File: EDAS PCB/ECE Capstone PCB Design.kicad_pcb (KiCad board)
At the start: 2 copper layers, 149.1 x 102.3 mm, 86 parts, among them J1 1053131105, J2 1053131105, J3 Conn_01x40_Socket, U1 MCP2518FDT-H/SL, U2 MCP2542FD-E/SN, U5 TPS562201, U6 TPS61165DBV, U7 TPS562201

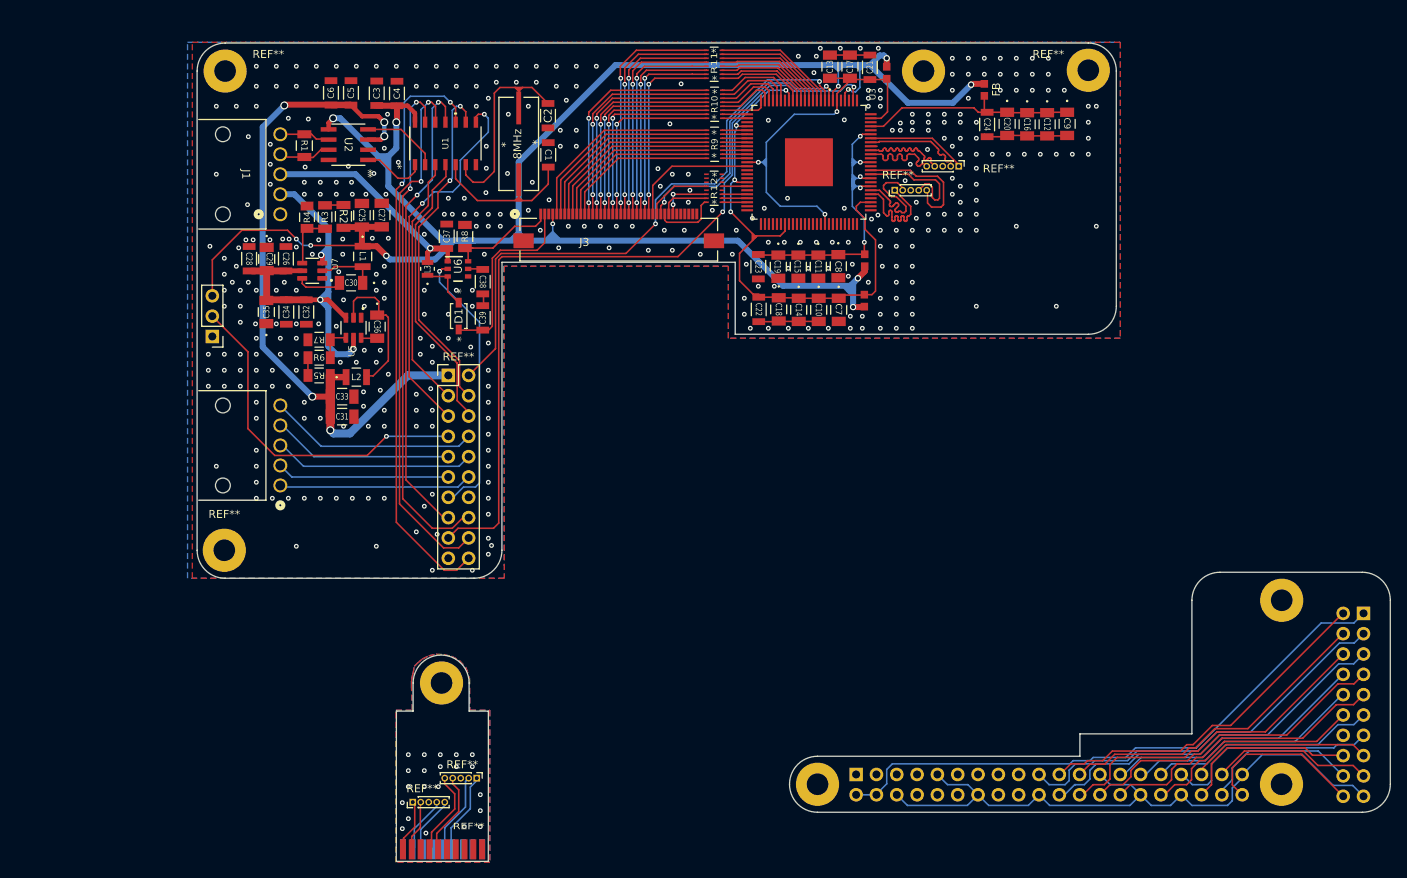
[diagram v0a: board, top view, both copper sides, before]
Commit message: Found a problem with one of the HDMI traces where the same net track spacing was to small. Corrected
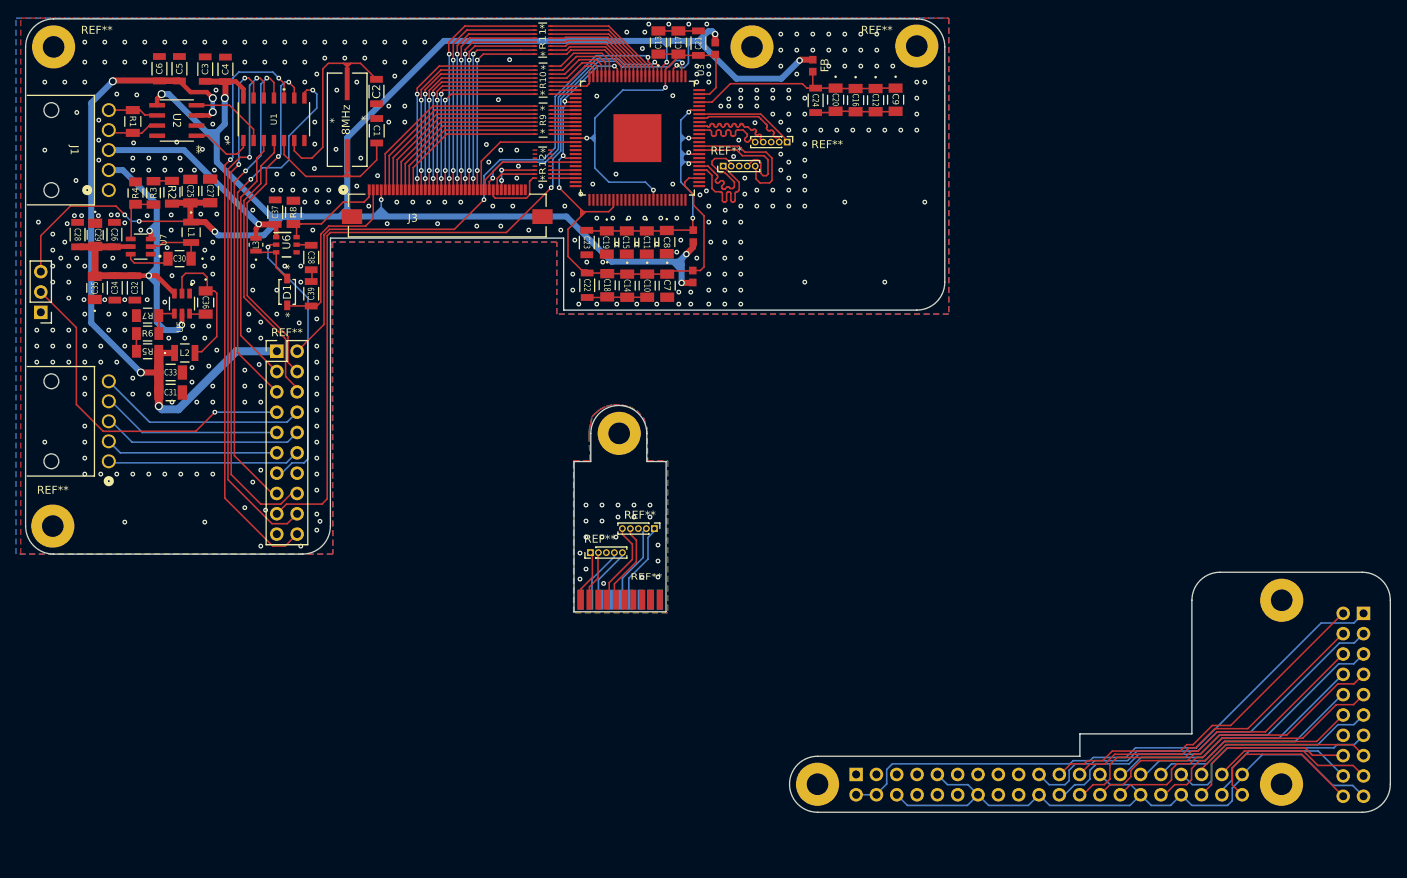
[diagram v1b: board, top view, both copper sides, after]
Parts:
- removed the ? at (153.1, 127.1)
- removed the ? at (213.4, 50.6)
- removed the REF** at (217.8, 62.5)
- removed the REF** at (149.6, 142.0)
- removed the REF** at (126.1, 50.6)
- removed the REF** at (157.6, 139.0)
- removed the REF** at (234.0, 50.5)
- removed the REF** at (209.8, 65.5)
- removed the REF** at (126.0, 110.5)
- added ?: , , F.Cu at (175.3, 95.9)
- added ?: , , F.Cu at (192.0, 47.6)
- added REF**: MountingHole_2.7mm_M2.5_Pad, MountingHole:MountingHole_2.7mm_M2.5_Pad, F.Cu at (212.6, 47.5)
- added REF**: MountingHole_2.7mm_M2.5_Pad, MountingHole:MountingHole_2.7mm_M2.5_Pad, F.Cu at (104.6, 107.5)
- added REF**: PinHeader_1x05_P1.00mm_Vertical, Connector_PinHeader_1.00mm:PinHeader_1x05_P1.00mm_Vertical, F.Cu at (188.4, 62.5)
- added REF**: PinHeader_1x05_P1.00mm_Vertical, Connector_PinHeader_1.00mm:PinHeader_1x05_P1.00mm_Vertical, F.Cu at (179.8, 107.8)
- added REF**: PinHeader_1x05_P1.00mm_Vertical, Connector_PinHeader_1.00mm:PinHeader_1x05_P1.00mm_Vertical, F.Cu at (171.8, 110.8)
- added REF**: MountingHole_2.7mm_M2.5_Pad, MountingHole:MountingHole_2.7mm_M2.5_Pad, F.Cu at (104.7, 47.6)
- added REF**: PinHeader_1x05_P1.00mm_Vertical, Connector_PinHeader_1.00mm:PinHeader_1x05_P1.00mm_Vertical, F.Cu at (196.4, 59.5)
- moved REF** 38.3 mm to (175.4, 120.3)
- moved R5 21.7 mm to (116.4, 85.6)
- moved R6 21.7 mm to (116.4, 83.4)
- moved C27 21.7 mm to (124.2, 65.6)
- moved C29 21.7 mm to (109.9, 71.1)
- moved C30 21.7 mm to (120.4, 74.1)
- moved C4 21.7 mm to (126.1, 50.4)
- moved C5 21.7 mm to (120.4, 50.3)
- moved C6 21.7 mm to (117.9, 50.3)
- moved L1 21.7 mm to (121.9, 70.8)
- moved C32 21.7 mm to (114.8, 77.7)
- moved C34 21.7 mm to (112.3, 77.7)
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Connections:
- 8MHz pad 1: Net-(U1-OSC2) -> (no net)
- 8MHz pad 2: Net-(U1-OSC1) -> (no net)
- C1 pad 1: /GND -> (no net)
- C1 pad 2: Net-(U1-OSC2) -> (no net)
- C10 pad 1: Net-(U3-OVDD) -> (no net)
- C10 pad 2: /GND -> (no net)
- C11 pad 1: Net-(U3-AVDD) -> (no net)
- C11 pad 2: /GND -> (no net)
- C12 pad 1: Net-(U3-PVDD) -> (no net)
- C12 pad 2: /GND -> (no net)
- C13 pad 1: Net-(U3-DVDD) -> (no net)
- C13 pad 2: /GND -> (no net)
- C14 pad 1: Net-(U3-OVDD) -> (no net)
- C14 pad 2: /GND -> (no net)
- C15 pad 1: Net-(U3-AVDD) -> (no net)
- C15 pad 2: /GND -> (no net)
- C16 pad 1: Net-(U3-PVDD) -> (no net)
- C16 pad 2: /GND -> (no net)
- C17 pad 1: Net-(U3-DVDD) -> (no net)
- C17 pad 2: /GND -> (no net)
- C18 pad 1: Net-(U3-OVDD) -> (no net)
- C18 pad 2: /GND -> (no net)
- C19 pad 1: Net-(U3-AVDD) -> (no net)
- C19 pad 2: /GND -> (no net)
- C2 pad 1: /GND -> (no net)
- C2 pad 2: Net-(U1-OSC1) -> (no net)
- C20 pad 1: Net-(U3-PVDD) -> (no net)
- C20 pad 2: /GND -> (no net)
- C21 pad 1: Net-(U3-DVDD) -> (no net)
- C21 pad 2: /GND -> (no net)
- C22 pad 1: Net-(U3-OVDD) -> (no net)
- C22 pad 2: /GND -> (no net)
- C23 pad 1: Net-(U3-AVDD) -> (no net)
- C23 pad 2: /GND -> (no net)
- C24 pad 1: Net-(U3-PVDD) -> (no net)
- C24 pad 2: /GND -> (no net)
- C25 pad 1: /GND -> (no net)
- C25 pad 2: +3.3V -> (no net)
- C26 pad 1: /GND -> (no net)
- C26 pad 2: 7V -> (no net)
- C27 pad 1: /GND -> (no net)
- C27 pad 2: +3.3V -> (no net)
- C28 pad 1: /GND -> (no net)
- C28 pad 2: 7V -> (no net)
- C29 pad 1: /GND -> (no net)
- C29 pad 2: 7V -> (no net)
- C3 pad 1: +3.3V -> (no net)
- C3 pad 2: /GND -> (no net)
- C30 pad 1: Net-(U7-SW) -> (no net)
- C30 pad 2: Net-(U7-VBST) -> (no net)
- C31 pad 1: +5V -> (no net)
- C31 pad 2: /GND -> (no net)
- C32 pad 1: /GND -> (no net)
- C32 pad 2: 7V -> (no net)
- C33 pad 1: +5V -> (no net)
- C33 pad 2: /GND -> (no net)
- C34 pad 1: /GND -> (no net)
- C34 pad 2: 7V -> (no net)
- C35 pad 1: /GND -> (no net)
- C35 pad 2: 7V -> (no net)
- C36 pad 1: Net-(U5-SW) -> (no net)
- C36 pad 2: Net-(U5-VBST) -> (no net)
- C37 pad 1: 12V -> (no net)
- C37 pad 2: /GND -> (no net)
- C38 pad 1: Net-(U6-COMP) -> (no net)
- C38 pad 2: /GND -> (no net)
- C39 pad 1: /LEDA -> (no net)
- C39 pad 2: /GND -> (no net)
- C4 pad 1: +3.3V -> (no net)
- C4 pad 2: /GND -> (no net)
- C5 pad 1: +5V -> (no net)
- C5 pad 2: /GND -> (no net)
- C6 pad 1: +5V -> (no net)
- C6 pad 2: /GND -> (no net)
- C7 pad 1: Net-(U3-OVDD) -> (no net)
- C7 pad 2: /GND -> (no net)
- C8 pad 1: Net-(U3-AVDD) -> (no net)
- C8 pad 2: /GND -> (no net)
- C9 pad 1: Net-(U3-PVDD) -> (no net)
- C9 pad 2: /GND -> (no net)
- D1 pad 1: /LEDA -> (no net)
- D1 pad 2: Net-(D1-ANODE) -> (no net)
- FB pad 1: +3.3V -> (no net)
- FB pad 2: Net-(U3-PVDD) -> (no net)
- FB1 pad 1: +3.3V -> (no net)
- FB1 pad 2: Net-(U3-OVDD) -> (no net)
- FB2 pad 1: +3.3V -> (no net)
- FB2 pad 2: Net-(U3-AVDD) -> (no net)
- FB4 pad 1: +3.3V -> (no net)
- FB4 pad 2: Net-(U3-DVDD) -> (no net)
- J1 pad 1: /GND -> (no net)
- J1 pad 2: 7V -> (no net)
- J1 pad 3: 12V -> (no net)
- J1 pad 4: /CAN Bus connection H -> (no net)
- J1 pad 5: /CAN Bus connection L -> (no net)
- J2 pad 1: BT4 -> (no net)
- J2 pad 2: BT3 -> (no net)
- J2 pad 3: BT2 -> (no net)
- J2 pad 4: BT1 -> (no net)
- J2 pad 5: BT0 -> (no net)
- J3 pad 1: /LEDK -> (no net)
- J3 pad 10: RO5 -> (no net)
- J3 pad 11: RO6 -> (no net)
- J3 pad 12: RO7 -> (no net)
- J3 pad 13: GO0 -> (no net)
- J3 pad 14: GO1 -> (no net)
- J3 pad 15: GO2 -> (no net)
- J3 pad 16: GO3 -> (no net)
- J3 pad 17: GO4 -> (no net)
- J3 pad 18: GO5 -> (no net)
- J3 pad 19: GO6 -> (no net)
- J3 pad 2: /LEDA -> (no net)
- J3 pad 20: GO7 -> (no net)
- J3 pad 21: BO0 -> (no net)
- J3 pad 22: BO1 -> (no net)
- J3 pad 23: BO2 -> (no net)
- J3 pad 24: BO3 -> (no net)
- J3 pad 25: BO4 -> (no net)
- J3 pad 26: BO5 -> (no net)
- J3 pad 27: BO6 -> (no net)
- J3 pad 28: BO7 -> (no net)
- J3 pad 29: /GND -> (no net)
- J3 pad 3: /GND -> (no net)
- J3 pad 30: PIXCLKOO -> (no net)
- J3 pad 31: /ACTIVE -> (no net)
- J3 pad 32: HSYNCO -> (no net)
- J3 pad 33: VSYNCO -> (no net)
- J3 pad 34: DISPENO -> (no net)
- J3 pad 35: unconnected-(J3-Pad35) -> (no net)
- J3 pad 36: unconnected-(J3-Pad36) -> (no net)
- J3 pad 37: unconnected-(J3-Pad37) -> (no net)
- J3 pad 38: unconnected-(J3-Pad38) -> (no net)
- J3 pad 39: unconnected-(J3-Pad39) -> (no net)
- J3 pad 4: +3.3V -> (no net)
- J3 pad 40: unconnected-(J3-Pad40) -> (no net)
- J3 pad 5: /RO0 -> (no net)
- J3 pad 6: RO1 -> (no net)
- J3 pad 7: RO2 -> (no net)
- J3 pad 8: RO3 -> (no net)
- J3 pad 9: RO4 -> (no net)
- L1 pad 1: +3.3V -> (no net)
- L1 pad 2: Net-(U7-SW) -> (no net)
- L2 pad 1: +5V -> (no net)
- L2 pad 2: Net-(U5-SW) -> (no net)
- L3 pad 1: Net-(D1-ANODE) -> (no net)
- L3 pad 2: 12V -> (no net)
- R1 pad 1: /CAN Bus connection L -> (no net)
- R1 pad 2: /CAN Bus connection H -> (no net)
- R10 pad 1: /G7 -> (no net)
- R10 pad 10: GO1 -> (no net)
- R10 pad 11: GO2 -> (no net)
- R10 pad 12: GO3 -> (no net)
- R10 pad 13: GO4 -> (no net)
- R10 pad 14: GO5 -> (no net)
- R10 pad 15: GO6 -> (no net)
- R10 pad 16: GO7 -> (no net)
- R10 pad 2: /G6 -> (no net)
- R10 pad 3: /G5 -> (no net)
- R10 pad 4: /G4 -> (no net)
- R10 pad 5: /G3 -> (no net)
- R10 pad 6: /G2 -> (no net)
- R10 pad 7: /G1 -> (no net)
- R10 pad 8: /G0 -> (no net)
- R10 pad 9: GO0 -> (no net)
- R11 pad 1: /B7 -> (no net)
- R11 pad 10: BO1 -> (no net)
- R11 pad 11: BO2 -> (no net)
- R11 pad 12: BO3 -> (no net)
- R11 pad 13: BO4 -> (no net)
- R11 pad 14: BO5 -> (no net)
- R11 pad 15: BO6 -> (no net)
- R11 pad 16: BO7 -> (no net)
- R11 pad 2: /B6 -> (no net)
- R11 pad 3: /B5 -> (no net)
- R11 pad 4: /B4 -> (no net)
- R11 pad 5: /B3 -> (no net)
- R11 pad 6: /B2 -> (no net)
- R11 pad 7: /B1 -> (no net)
- R11 pad 8: /B0 -> (no net)
- R11 pad 9: BO0 -> (no net)
- R12 pad 1: /HSYNC -> (no net)
- R12 pad 10: /GND -> (no net)
- R12 pad 11: /GND -> (no net)
- R12 pad 12: PIXCLKOO -> (no net)
- R12 pad 13: /GND -> (no net)
- R12 pad 14: DISPENO -> (no net)
- R12 pad 15: VSYNCO -> (no net)
- R12 pad 16: HSYNCO -> (no net)
- R12 pad 2: /VSYNC -> (no net)
- R12 pad 3: /DISPEN -> (no net)
- R12 pad 4: /GND -> (no net)
- R12 pad 5: /PIXCLK -> (no net)
- R12 pad 6: /GND -> (no net)
- R12 pad 7: /GND -> (no net)
- R12 pad 8: /GND -> (no net)
- R12 pad 9: /GND -> (no net)
- R2 pad 1: Net-(R2-Pad1) -> (no net)
- R2 pad 2: +3.3V -> (no net)
- R3 pad 1: Net-(U7-VFB) -> (no net)
- R3 pad 2: Net-(R2-Pad1) -> (no net)
- R4 pad 1: Net-(U7-VFB) -> (no net)
- R4 pad 2: /GND -> (no net)
- R5 pad 1: +5V -> (no net)
- R5 pad 2: Net-(R5-Pad2) -> (no net)
- R6 pad 1: Net-(R5-Pad2) -> (no net)
- R6 pad 2: Net-(U5-VFB) -> (no net)
- R7 pad 1: Net-(U5-VFB) -> (no net)
- R7 pad 2: /GND -> (no net)
- R8 pad 1: /LEDK -> (no net)
- R8 pad 2: /GND -> (no net)
- R9 pad 1: /R7 -> (no net)
- R9 pad 10: RO1 -> (no net)
- R9 pad 11: RO2 -> (no net)
- R9 pad 12: RO3 -> (no net)
- R9 pad 13: RO4 -> (no net)
- R9 pad 14: RO5 -> (no net)
- R9 pad 15: RO6 -> (no net)
- R9 pad 16: RO7 -> (no net)
- R9 pad 2: /R6 -> (no net)
- R9 pad 3: /R5 -> (no net)
- R9 pad 4: /R4 -> (no net)
- R9 pad 5: /R3 -> (no net)
- R9 pad 6: /R2 -> (no net)
- R9 pad 7: /R1 -> (no net)
- R9 pad 8: /R0 -> (no net)
- R9 pad 9: /RO0 -> (no net)
- REF** pad 1: +5V -> (no net)
- REF** pad 10: BT2 -> (no net)
- REF** pad 11: BT3 -> (no net)
- REF** pad 12: BT4 -> (no net)
- REF** pad 13: /PWM -> (no net)
- REF** pad 15: /Rasberry PI (SPI input) -> (no net)
- REF** pad 16: /Rasberry PI (chip select) -> (no net)
- REF** pad 17: /PWRON -> (no net)
- REF** pad 18: /Rasberry PI (SPI output) -> (no net)
- REF** pad 19: /GND -> (no net)
- REF** pad 2: /PWRON_D -> (no net)
- REF** pad 20: /Rasberry PI (SPI clock input) -> (no net)
- REF** pad 3: /Rasberry PI (clock output) -> (no net)
- REF** pad 4: /Rasberry PI (RX interupt active low) -> (no net)
- REF** pad 5: /Rasberry PI (TX interupt active low) -> (no net)
- REF** pad 6: /Rasberry PI (interupt active low) -> (no net)
- REF** pad 7: Net-(J3-Pad5) -> (no net)
- REF** pad 8: BT0 -> (no net)
- REF** pad 9: BT1 -> (no net)
- REF** pad 1: /GND -> (no net)
- REF** pad 2: Net-(J3-Pad5) -> (no net)
- REF** pad 3: +3.3V -> (no net)
- REF** pad 1: TDMS2+ -> (no net)
- REF** pad 10: TDMSCLK+ -> (no net)
- REF** pad 11: DGND -> (no net)
- REF** pad 12: TDMSCLK- -> (no net)
- REF** pad 17: DGND -> (no net)
- REF** pad 18: D+5V -> (no net)
- REF** pad 2: DGND -> (no net)
- REF** pad 3: TDMS2- -> (no net)
- REF** pad 4: TDMS1+ -> (no net)
- REF** pad 5: DGND -> (no net)
- REF** pad 6: TDMS1- -> (no net)
- REF** pad 7: TDMS0+ -> (no net)
- REF** pad 8: DGND -> (no net)
- REF** pad 9: TDMS0- -> (no net)
- U1 pad 1: /TX -> (no net)
- U1 pad 10: /Rasberry PI (SPI clock input) -> (no net)
- U1 pad 11: /Rasberry PI (SPI input) -> (no net)
- U1 pad 12: /Rasberry PI (SPI output) -> (no net)
- U1 pad 13: /Rasberry PI (chip select) -> (no net)
- U1 pad 14: +3.3V -> (no net)
- U1 pad 2: /RX -> (no net)
- U1 pad 3: /Rasberry PI (clock output) -> (no net)
- U1 pad 4: /Rasberry PI (interupt active low) -> (no net)
- U1 pad 5: Net-(U1-OSC2) -> (no net)
- U1 pad 6: Net-(U1-OSC1) -> (no net)
- U1 pad 7: /GND -> (no net)
- U1 pad 8: /Rasberry PI (TX interupt active low) -> (no net)
- U1 pad 9: /Rasberry PI (RX interupt active low) -> (no net)
- U2 pad 1: /TX -> (no net)
- U2 pad 2: /GND -> (no net)
- U2 pad 3: +5V -> (no net)
- U2 pad 4: /RX -> (no net)
- U2 pad 5: +3.3V -> (no net)
- U2 pad 6: /CAN Bus connection L -> (no net)
- U2 pad 7: /CAN Bus connection H -> (no net)
- U2 pad 8: /GND -> (no net)
- U3 pad 1: /GND -> (no net)
- U3 pad 10: /B0 -> (no net)
- U3 pad 100: /GND -> (no net)
- U3 pad 101: unconnected-(U3-EPAD-Pad101) -> (no net)
- U3 pad 11: /B1 -> (no net)
- U3 pad 12: /B2 -> (no net)
- U3 pad 13: /B3 -> (no net)
- U3 pad 14: /B4 -> (no net)
- U3 pad 15: /B5 -> (no net)
- U3 pad 16: /B6 -> (no net)
- U3 pad 17: /B7 -> (no net)
- U3 pad 18: Net-(U3-OVDD) -> (no net)
- U3 pad 19: /GND -> (no net)
- U3 pad 2: /PWRON -> (no net)
- U3 pad 20: /G0 -> (no net)
- U3 pad 21: /G1 -> (no net)
- U3 pad 22: /G2 -> (no net)
- U3 pad 23: /G3 -> (no net)
- U3 pad 24: /G4 -> (no net)
- U3 pad 25: /G5 -> (no net)
- U3 pad 26: /G6 -> (no net)
- U3 pad 27: /G7 -> (no net)
- U3 pad 28: /GND -> (no net)
- U3 pad 29: Net-(U3-OVDD) -> (no net)
- U3 pad 3: /GND -> (no net)
- U3 pad 30: /R0 -> (no net)
- U3 pad 31: /R1 -> (no net)
- U3 pad 32: /R2 -> (no net)
- U3 pad 33: /R3 -> (no net)
- U3 pad 34: /R4 -> (no net)
- U3 pad 35: /R5 -> (no net)
- U3 pad 36: /R6 -> (no net)
- U3 pad 37: /R7 -> (no net)
- U3 pad 38: Net-(U3-DVDD) -> (no net)
- U3 pad 39: /GND -> (no net)
- U3 pad 4: +3.3V -> (no net)
- U3 pad 40: unconnected-(U3-CTL1-Pad40) -> (no net)
- U3 pad 41: unconnected-(U3-CTL2-Pad41) -> (no net)
- U3 pad 42: unconnected-(U3-CTL3-Pad42) -> (no net)
- U3 pad 43: Net-(U3-OVDD) -> (no net)
- U3 pad 44: /PIXCLK -> (no net)
- U3 pad 45: /GND -> (no net)
- U3 pad 46: /DISPEN -> (no net)
- U3 pad 47: /VSYNC -> (no net)
- U3 pad 48: /HSYNC -> (no net)
- U3 pad 49: unconnected-(U3-QO0-Pad49) -> (no net)
- U3 pad 5: /GND -> (no net)
- U3 pad 50: unconnected-(U3-QO1-Pad50) -> (no net)
- U3 pad 51: unconnected-(U3-QO2-Pad51) -> (no net)
- U3 pad 52: unconnected-(U3-QO3-Pad52) -> (no net)
- U3 pad 53: unconnected-(U3-QO4-Pad53) -> (no net)
- U3 pad 54: unconnected-(U3-QO5-Pad54) -> (no net)
- U3 pad 55: unconnected-(U3-QO6-Pad55) -> (no net)
- U3 pad 56: unconnected-(U3-QO7-Pad56) -> (no net)
- U3 pad 57: Net-(U3-OVDD) -> (no net)
- U3 pad 58: /GND -> (no net)
- U3 pad 59: unconnected-(U3-QO8-Pad59) -> (no net)
- U3 pad 6: Net-(U3-DVDD) -> (no net)
- U3 pad 60: unconnected-(U3-QO9-Pad60) -> (no net)
- U3 pad 61: unconnected-(U3-QO10-Pad61) -> (no net)
- U3 pad 62: unconnected-(U3-QO11-Pad62) -> (no net)
- U3 pad 63: unconnected-(U3-QO12-Pad63) -> (no net)
- U3 pad 64: unconnected-(U3-QO13-Pad64) -> (no net)
- U3 pad 65: unconnected-(U3-QO14-Pad65) -> (no net)
- U3 pad 66: unconnected-(U3-QO15-Pad66) -> (no net)
- U3 pad 67: Net-(U3-DVDD) -> (no net)
- U3 pad 68: /GND -> (no net)
- U3 pad 69: unconnected-(U3-QO16-Pad69) -> (no net)
- U3 pad 7: +3.3V -> (no net)
- U3 pad 70: unconnected-(U3-QO17-Pad70) -> (no net)
- U3 pad 71: unconnected-(U3-QO18-Pad71) -> (no net)
- U3 pad 72: unconnected-(U3-QO19-Pad72) -> (no net)
- U3 pad 73: unconnected-(U3-QO20-Pad73) -> (no net)
- U3 pad 74: unconnected-(U3-QO21-Pad74) -> (no net)
- U3 pad 75: unconnected-(U3-QO22-Pad75) -> (no net)
- U3 pad 76: /GND -> (no net)
- U3 pad 77: unconnected-(U3-QO23-Pad77) -> (no net)
- U3 pad 78: Net-(U3-OVDD) -> (no net)
- U3 pad 79: /GND -> (no net)
- U3 pad 8: /ACTIVE -> (no net)
- U3 pad 80: Net-(U3-RX2+) -> (no net)
- U3 pad 81: Net-(U3-RX2-) -> (no net)
- U3 pad 82: Net-(U3-AVDD) -> (no net)
- U3 pad 83: /GND -> (no net)
- U3 pad 84: Net-(U3-AVDD) -> (no net)
- U3 pad 85: Net-(U3-RX1+) -> (no net)
- U3 pad 86: Net-(U3-RX1-) -> (no net)
- U3 pad 87: /GND -> (no net)
- U3 pad 88: Net-(U3-AVDD) -> (no net)
- U3 pad 89: /GND -> (no net)
- U3 pad 9: /PWRON_D -> (no net)
- U3 pad 90: Net-(U3-RX0+) -> (no net)
- U3 pad 91: Net-(U3-RX0-) -> (no net)
- U3 pad 92: /GND -> (no net)
- U3 pad 93: Net-(U3-RXC+) -> (no net)
- U3 pad 94: Net-(U3-RXC-) -> (no net)
- U3 pad 95: Net-(U3-AVDD) -> (no net)
- U3 pad 96: unconnected-(U3-EXT_RES-Pad96) -> (no net)
- U3 pad 97: Net-(U3-PVDD) -> (no net)
- U3 pad 98: /GND -> (no net)
- U3 pad 99: Net-(U3-DVDD) -> (no net)
- U5 pad 1: /GND -> (no net)
- U5 pad 2: Net-(U5-SW) -> (no net)
- U5 pad 3: 7V -> (no net)
- U5 pad 4: Net-(U5-VFB) -> (no net)
- U5 pad 5: 7V -> (no net)
- U5 pad 6: Net-(U5-VBST) -> (no net)
- U6 pad 1: 12V -> (no net)
- U6 pad 2: /PWM -> (no net)
- U6 pad 3: Net-(D1-ANODE) -> (no net)
- U6 pad 4: /GND -> (no net)
- U6 pad 5: Net-(U6-COMP) -> (no net)
- U6 pad 6: /LEDK -> (no net)
- U7 pad 1: /GND -> (no net)
- U7 pad 2: Net-(U7-SW) -> (no net)
- U7 pad 3: 7V -> (no net)
- U7 pad 4: Net-(U7-VFB) -> (no net)
- U7 pad 5: 7V -> (no net)
- U7 pad 6: Net-(U7-VBST) -> (no net)
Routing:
- net (no net): track 0.00 -> 2667.7 mm, vias 0 -> 495
- net +3.3V: track 242.0 -> 0.00 mm, vias 12 -> 0
- net /PWRON: track 101.7 -> 0.00 mm, vias 2 -> 0
- net +5V: track 89.1 -> 0.00 mm, vias 5 -> 0
- net /Rasberry PI (SPI clock input): track 74.2 -> 0.00 mm, vias 2 -> 0
- net /PWRON_D: track 74.0 -> 0.00 mm, vias 2 -> 0
- net Net-(U3-OVDD): track 70.9 -> 0.00 mm, vias 4 -> 0
- net /Rasberry PI (SPI output): track 66.9 -> 0.00 mm, vias 2 -> 0
- net /Rasberry PI (chip select): track 63.8 -> 0.00 mm, vias 2 -> 0
- net /Rasberry PI (SPI input): track 59.2 -> 0.00 mm, vias 2 -> 0
- net 7V: track 58.7 -> 0.00 mm, vias 3 -> 0
- net /Rasberry PI (TX interupt active low): track 47.3 -> 0.00 mm, vias 2 -> 0
- net Net-(U3-DVDD): track 47.0 -> 0.00 mm, vias 3 -> 0
- net /Rasberry PI (RX interupt active low): track 43.5 -> 0.00 mm, vias 2 -> 0
- net Net-(J3-Pad5): track 43.3 -> 0.00 mm, vias 1 -> 0
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- added copper zone on B.Cu, net (none)
- added copper zone on F.Cu, net (none)
- removed copper zone on B.Cu, net /GND
- removed copper zone on F.Cu, net /GND
- removed copper zone on B.Cu, net DGND
- removed copper zone on F.Cu, net DGND
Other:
- board size 149.1 x 102.3 mm -> 170.6 x 99.2 mm

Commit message: Updated main to match recovery-branch
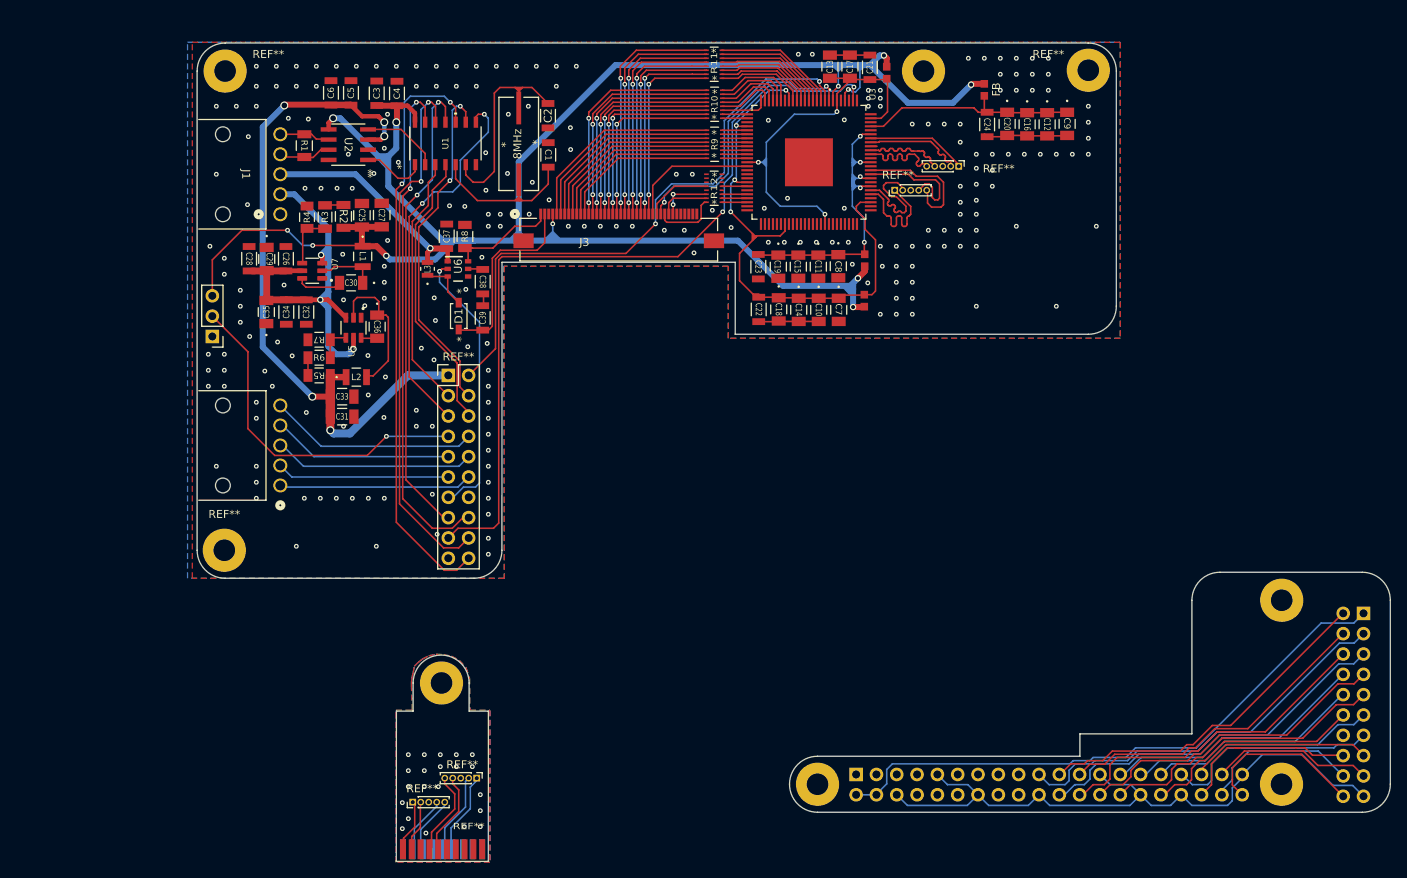
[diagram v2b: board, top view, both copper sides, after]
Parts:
- removed the ? at (175.3, 95.9)
- removed the ? at (192.0, 47.6)
- removed the REF** at (212.6, 47.5)
- removed the REF** at (104.6, 107.5)
- removed the REF** at (188.4, 62.5)
- removed the REF** at (179.8, 107.8)
- removed the REF** at (171.8, 110.8)
- removed the REF** at (104.7, 47.6)
- removed the REF** at (196.4, 59.5)
- added ?: , , F.Cu at (153.1, 127.1)
- added ?: , , F.Cu at (213.4, 50.6)
- added REF**: PinHeader_1x05_P1.00mm_Vertical, Connector_PinHeader_1.00mm:PinHeader_1x05_P1.00mm_Vertical, F.Cu at (217.8, 62.5)
- added REF**: PinHeader_1x05_P1.00mm_Vertical, Connector_PinHeader_1.00mm:PinHeader_1x05_P1.00mm_Vertical, F.Cu at (149.6, 142.0)
- added REF**: MountingHole_2.7mm_M2.5_Pad, MountingHole:MountingHole_2.7mm_M2.5_Pad, F.Cu at (126.1, 50.6)
- added REF**: PinHeader_1x05_P1.00mm_Vertical, Connector_PinHeader_1.00mm:PinHeader_1x05_P1.00mm_Vertical, F.Cu at (157.6, 139.0)
- added REF**: MountingHole_2.7mm_M2.5_Pad, MountingHole:MountingHole_2.7mm_M2.5_Pad, F.Cu at (234.0, 50.5)
- added REF**: PinHeader_1x05_P1.00mm_Vertical, Connector_PinHeader_1.00mm:PinHeader_1x05_P1.00mm_Vertical, F.Cu at (209.8, 65.5)
- added REF**: MountingHole_2.7mm_M2.5_Pad, MountingHole:MountingHole_2.7mm_M2.5_Pad, F.Cu at (126.0, 110.5)
- moved REF** 38.3 mm to (153.2, 151.5)
- moved R5 21.7 mm to (137.9, 88.7)
- moved R6 21.7 mm to (137.9, 86.4)
- moved C27 21.7 mm to (145.7, 68.6)
- moved C29 21.7 mm to (131.3, 74.1)
- moved C30 21.7 mm to (141.8, 77.1)
- moved C4 21.7 mm to (147.6, 53.4)
- moved C5 21.7 mm to (141.8, 53.3)
- moved C6 21.7 mm to (139.3, 53.3)
- moved L1 21.7 mm to (143.3, 73.8)
- moved C32 21.7 mm to (136.2, 80.7)
- moved C34 21.7 mm to (133.8, 80.7)
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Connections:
- 8MHz pad 1: (no net) -> Net-(U1-OSC2)
- 8MHz pad 2: (no net) -> Net-(U1-OSC1)
- C1 pad 1: (no net) -> /GND
- C1 pad 2: (no net) -> Net-(U1-OSC2)
- C10 pad 1: (no net) -> Net-(U3-OVDD)
- C10 pad 2: (no net) -> /GND
- C11 pad 1: (no net) -> Net-(U3-AVDD)
- C11 pad 2: (no net) -> /GND
- C12 pad 1: (no net) -> Net-(U3-PVDD)
- C12 pad 2: (no net) -> /GND
- C13 pad 1: (no net) -> Net-(U3-DVDD)
- C13 pad 2: (no net) -> /GND
- C14 pad 1: (no net) -> Net-(U3-OVDD)
- C14 pad 2: (no net) -> /GND
- C15 pad 1: (no net) -> Net-(U3-AVDD)
- C15 pad 2: (no net) -> /GND
- C16 pad 1: (no net) -> Net-(U3-PVDD)
- C16 pad 2: (no net) -> /GND
- C17 pad 1: (no net) -> Net-(U3-DVDD)
- C17 pad 2: (no net) -> /GND
- C18 pad 1: (no net) -> Net-(U3-OVDD)
- C18 pad 2: (no net) -> /GND
- C19 pad 1: (no net) -> Net-(U3-AVDD)
- C19 pad 2: (no net) -> /GND
- C2 pad 1: (no net) -> /GND
- C2 pad 2: (no net) -> Net-(U1-OSC1)
- C20 pad 1: (no net) -> Net-(U3-PVDD)
- C20 pad 2: (no net) -> /GND
- C21 pad 1: (no net) -> Net-(U3-DVDD)
- C21 pad 2: (no net) -> /GND
- C22 pad 1: (no net) -> Net-(U3-OVDD)
- C22 pad 2: (no net) -> /GND
- C23 pad 1: (no net) -> Net-(U3-AVDD)
- C23 pad 2: (no net) -> /GND
- C24 pad 1: (no net) -> Net-(U3-PVDD)
- C24 pad 2: (no net) -> /GND
- C25 pad 1: (no net) -> /GND
- C25 pad 2: (no net) -> +3.3V
- C26 pad 1: (no net) -> /GND
- C26 pad 2: (no net) -> 7V
- C27 pad 1: (no net) -> /GND
- C27 pad 2: (no net) -> +3.3V
- C28 pad 1: (no net) -> /GND
- C28 pad 2: (no net) -> 7V
- C29 pad 1: (no net) -> /GND
- C29 pad 2: (no net) -> 7V
- C3 pad 1: (no net) -> +3.3V
- C3 pad 2: (no net) -> /GND
- C30 pad 1: (no net) -> Net-(U7-SW)
- C30 pad 2: (no net) -> Net-(U7-VBST)
- C31 pad 1: (no net) -> +5V
- C31 pad 2: (no net) -> /GND
- C32 pad 1: (no net) -> /GND
- C32 pad 2: (no net) -> 7V
- C33 pad 1: (no net) -> +5V
- C33 pad 2: (no net) -> /GND
- C34 pad 1: (no net) -> /GND
- C34 pad 2: (no net) -> 7V
- C35 pad 1: (no net) -> /GND
- C35 pad 2: (no net) -> 7V
- C36 pad 1: (no net) -> Net-(U5-SW)
- C36 pad 2: (no net) -> Net-(U5-VBST)
- C37 pad 1: (no net) -> 12V
- C37 pad 2: (no net) -> /GND
- C38 pad 1: (no net) -> Net-(U6-COMP)
- C38 pad 2: (no net) -> /GND
- C39 pad 1: (no net) -> /LEDA
- C39 pad 2: (no net) -> /GND
- C4 pad 1: (no net) -> +3.3V
- C4 pad 2: (no net) -> /GND
- C5 pad 1: (no net) -> +5V
- C5 pad 2: (no net) -> /GND
- C6 pad 1: (no net) -> +5V
- C6 pad 2: (no net) -> /GND
- C7 pad 1: (no net) -> Net-(U3-OVDD)
- C7 pad 2: (no net) -> /GND
- C8 pad 1: (no net) -> Net-(U3-AVDD)
- C8 pad 2: (no net) -> /GND
- C9 pad 1: (no net) -> Net-(U3-PVDD)
- C9 pad 2: (no net) -> /GND
- D1 pad 1: (no net) -> /LEDA
- D1 pad 2: (no net) -> Net-(D1-ANODE)
- FB pad 1: (no net) -> +3.3V
- FB pad 2: (no net) -> Net-(U3-PVDD)
- FB1 pad 1: (no net) -> +3.3V
- FB1 pad 2: (no net) -> Net-(U3-OVDD)
- FB2 pad 1: (no net) -> +3.3V
- FB2 pad 2: (no net) -> Net-(U3-AVDD)
- FB4 pad 1: (no net) -> +3.3V
- FB4 pad 2: (no net) -> Net-(U3-DVDD)
- J1 pad 1: (no net) -> /GND
- J1 pad 2: (no net) -> 7V
- J1 pad 3: (no net) -> 12V
- J1 pad 4: (no net) -> /CAN Bus connection H
- J1 pad 5: (no net) -> /CAN Bus connection L
- J2 pad 1: (no net) -> BT4
- J2 pad 2: (no net) -> BT3
- J2 pad 3: (no net) -> BT2
- J2 pad 4: (no net) -> BT1
- J2 pad 5: (no net) -> BT0
- J3 pad 1: (no net) -> /LEDK
- J3 pad 10: (no net) -> RO5
- J3 pad 11: (no net) -> RO6
- J3 pad 12: (no net) -> RO7
- J3 pad 13: (no net) -> GO0
- J3 pad 14: (no net) -> GO1
- J3 pad 15: (no net) -> GO2
- J3 pad 16: (no net) -> GO3
- J3 pad 17: (no net) -> GO4
- J3 pad 18: (no net) -> GO5
- J3 pad 19: (no net) -> GO6
- J3 pad 2: (no net) -> /LEDA
- J3 pad 20: (no net) -> GO7
- J3 pad 21: (no net) -> BO0
- J3 pad 22: (no net) -> BO1
- J3 pad 23: (no net) -> BO2
- J3 pad 24: (no net) -> BO3
- J3 pad 25: (no net) -> BO4
- J3 pad 26: (no net) -> BO5
- J3 pad 27: (no net) -> BO6
- J3 pad 28: (no net) -> BO7
- J3 pad 29: (no net) -> /GND
- J3 pad 3: (no net) -> /GND
- J3 pad 30: (no net) -> PIXCLKOO
- J3 pad 31: (no net) -> /ACTIVE
- J3 pad 32: (no net) -> HSYNCO
- J3 pad 33: (no net) -> VSYNCO
- J3 pad 34: (no net) -> DISPENO
- J3 pad 35: (no net) -> unconnected-(J3-Pad35)
- J3 pad 36: (no net) -> unconnected-(J3-Pad36)
- J3 pad 37: (no net) -> unconnected-(J3-Pad37)
- J3 pad 38: (no net) -> unconnected-(J3-Pad38)
- J3 pad 39: (no net) -> unconnected-(J3-Pad39)
- J3 pad 4: (no net) -> +3.3V
- J3 pad 40: (no net) -> unconnected-(J3-Pad40)
- J3 pad 5: (no net) -> /RO0
- J3 pad 6: (no net) -> RO1
- J3 pad 7: (no net) -> RO2
- J3 pad 8: (no net) -> RO3
- J3 pad 9: (no net) -> RO4
- L1 pad 1: (no net) -> +3.3V
- L1 pad 2: (no net) -> Net-(U7-SW)
- L2 pad 1: (no net) -> +5V
- L2 pad 2: (no net) -> Net-(U5-SW)
- L3 pad 1: (no net) -> Net-(D1-ANODE)
- L3 pad 2: (no net) -> 12V
- R1 pad 1: (no net) -> /CAN Bus connection L
- R1 pad 2: (no net) -> /CAN Bus connection H
- R10 pad 1: (no net) -> /G7
- R10 pad 10: (no net) -> GO1
- R10 pad 11: (no net) -> GO2
- R10 pad 12: (no net) -> GO3
- R10 pad 13: (no net) -> GO4
- R10 pad 14: (no net) -> GO5
- R10 pad 15: (no net) -> GO6
- R10 pad 16: (no net) -> GO7
- R10 pad 2: (no net) -> /G6
- R10 pad 3: (no net) -> /G5
- R10 pad 4: (no net) -> /G4
- R10 pad 5: (no net) -> /G3
- R10 pad 6: (no net) -> /G2
- R10 pad 7: (no net) -> /G1
- R10 pad 8: (no net) -> /G0
- R10 pad 9: (no net) -> GO0
- R11 pad 1: (no net) -> /B7
- R11 pad 10: (no net) -> BO1
- R11 pad 11: (no net) -> BO2
- R11 pad 12: (no net) -> BO3
- R11 pad 13: (no net) -> BO4
- R11 pad 14: (no net) -> BO5
- R11 pad 15: (no net) -> BO6
- R11 pad 16: (no net) -> BO7
- R11 pad 2: (no net) -> /B6
- R11 pad 3: (no net) -> /B5
- R11 pad 4: (no net) -> /B4
- R11 pad 5: (no net) -> /B3
- R11 pad 6: (no net) -> /B2
- R11 pad 7: (no net) -> /B1
- R11 pad 8: (no net) -> /B0
- R11 pad 9: (no net) -> BO0
- R12 pad 1: (no net) -> /HSYNC
- R12 pad 10: (no net) -> /GND
- R12 pad 11: (no net) -> /GND
- R12 pad 12: (no net) -> PIXCLKOO
- R12 pad 13: (no net) -> /GND
- R12 pad 14: (no net) -> DISPENO
- R12 pad 15: (no net) -> VSYNCO
- R12 pad 16: (no net) -> HSYNCO
- R12 pad 2: (no net) -> /VSYNC
- R12 pad 3: (no net) -> /DISPEN
- R12 pad 4: (no net) -> /GND
- R12 pad 5: (no net) -> /PIXCLK
- R12 pad 6: (no net) -> /GND
- R12 pad 7: (no net) -> /GND
- R12 pad 8: (no net) -> /GND
- R12 pad 9: (no net) -> /GND
- R2 pad 1: (no net) -> Net-(R2-Pad1)
- R2 pad 2: (no net) -> +3.3V
- R3 pad 1: (no net) -> Net-(U7-VFB)
- R3 pad 2: (no net) -> Net-(R2-Pad1)
- R4 pad 1: (no net) -> Net-(U7-VFB)
- R4 pad 2: (no net) -> /GND
- R5 pad 1: (no net) -> +5V
- R5 pad 2: (no net) -> Net-(R5-Pad2)
- R6 pad 1: (no net) -> Net-(R5-Pad2)
- R6 pad 2: (no net) -> Net-(U5-VFB)
- R7 pad 1: (no net) -> Net-(U5-VFB)
- R7 pad 2: (no net) -> /GND
- R8 pad 1: (no net) -> /LEDK
- R8 pad 2: (no net) -> /GND
- R9 pad 1: (no net) -> /R7
- R9 pad 10: (no net) -> RO1
- R9 pad 11: (no net) -> RO2
- R9 pad 12: (no net) -> RO3
- R9 pad 13: (no net) -> RO4
- R9 pad 14: (no net) -> RO5
- R9 pad 15: (no net) -> RO6
- R9 pad 16: (no net) -> RO7
- R9 pad 2: (no net) -> /R6
- R9 pad 3: (no net) -> /R5
- R9 pad 4: (no net) -> /R4
- R9 pad 5: (no net) -> /R3
- R9 pad 6: (no net) -> /R2
- R9 pad 7: (no net) -> /R1
- R9 pad 8: (no net) -> /R0
- R9 pad 9: (no net) -> /RO0
- REF** pad 1: (no net) -> +5V
- REF** pad 10: (no net) -> BT2
- REF** pad 11: (no net) -> BT3
- REF** pad 12: (no net) -> BT4
- REF** pad 13: (no net) -> /PWM
- REF** pad 15: (no net) -> /Rasberry PI (SPI input)
- REF** pad 16: (no net) -> /Rasberry PI (chip select)
- REF** pad 17: (no net) -> /PWRON
- REF** pad 18: (no net) -> /Rasberry PI (SPI output)
- REF** pad 19: (no net) -> /GND
- REF** pad 2: (no net) -> /PWRON_D
- REF** pad 20: (no net) -> /Rasberry PI (SPI clock input)
- REF** pad 3: (no net) -> /Rasberry PI (clock output)
- REF** pad 4: (no net) -> /Rasberry PI (RX interupt active low)
- REF** pad 5: (no net) -> /Rasberry PI (TX interupt active low)
- REF** pad 6: (no net) -> /Rasberry PI (interupt active low)
- REF** pad 7: (no net) -> Net-(J3-Pad5)
- REF** pad 8: (no net) -> BT0
- REF** pad 9: (no net) -> BT1
- REF** pad 1: (no net) -> /GND
- REF** pad 2: (no net) -> Net-(J3-Pad5)
- REF** pad 3: (no net) -> +3.3V
- REF** pad 1: (no net) -> TDMS2+
- REF** pad 10: (no net) -> TDMSCLK+
- REF** pad 11: (no net) -> DGND
- REF** pad 12: (no net) -> TDMSCLK-
- REF** pad 17: (no net) -> DGND
- REF** pad 18: (no net) -> D+5V
- REF** pad 2: (no net) -> DGND
- REF** pad 3: (no net) -> TDMS2-
- REF** pad 4: (no net) -> TDMS1+
- REF** pad 5: (no net) -> DGND
- REF** pad 6: (no net) -> TDMS1-
- REF** pad 7: (no net) -> TDMS0+
- REF** pad 8: (no net) -> DGND
- REF** pad 9: (no net) -> TDMS0-
- U1 pad 1: (no net) -> /TX
- U1 pad 10: (no net) -> /Rasberry PI (SPI clock input)
- U1 pad 11: (no net) -> /Rasberry PI (SPI input)
- U1 pad 12: (no net) -> /Rasberry PI (SPI output)
- U1 pad 13: (no net) -> /Rasberry PI (chip select)
- U1 pad 14: (no net) -> +3.3V
- U1 pad 2: (no net) -> /RX
- U1 pad 3: (no net) -> /Rasberry PI (clock output)
- U1 pad 4: (no net) -> /Rasberry PI (interupt active low)
- U1 pad 5: (no net) -> Net-(U1-OSC2)
- U1 pad 6: (no net) -> Net-(U1-OSC1)
- U1 pad 7: (no net) -> /GND
- U1 pad 8: (no net) -> /Rasberry PI (TX interupt active low)
- U1 pad 9: (no net) -> /Rasberry PI (RX interupt active low)
- U2 pad 1: (no net) -> /TX
- U2 pad 2: (no net) -> /GND
- U2 pad 3: (no net) -> +5V
- U2 pad 4: (no net) -> /RX
- U2 pad 5: (no net) -> +3.3V
- U2 pad 6: (no net) -> /CAN Bus connection L
- U2 pad 7: (no net) -> /CAN Bus connection H
- U2 pad 8: (no net) -> /GND
- U3 pad 1: (no net) -> /GND
- U3 pad 10: (no net) -> /B0
- U3 pad 100: (no net) -> /GND
- U3 pad 101: (no net) -> unconnected-(U3-EPAD-Pad101)
- U3 pad 11: (no net) -> /B1
- U3 pad 12: (no net) -> /B2
- U3 pad 13: (no net) -> /B3
- U3 pad 14: (no net) -> /B4
- U3 pad 15: (no net) -> /B5
- U3 pad 16: (no net) -> /B6
- U3 pad 17: (no net) -> /B7
- U3 pad 18: (no net) -> Net-(U3-OVDD)
- U3 pad 19: (no net) -> /GND
- U3 pad 2: (no net) -> /PWRON
- U3 pad 20: (no net) -> /G0
- U3 pad 21: (no net) -> /G1
- U3 pad 22: (no net) -> /G2
- U3 pad 23: (no net) -> /G3
- U3 pad 24: (no net) -> /G4
- U3 pad 25: (no net) -> /G5
- U3 pad 26: (no net) -> /G6
- U3 pad 27: (no net) -> /G7
- U3 pad 28: (no net) -> /GND
- U3 pad 29: (no net) -> Net-(U3-OVDD)
- U3 pad 3: (no net) -> /GND
- U3 pad 30: (no net) -> /R0
- U3 pad 31: (no net) -> /R1
- U3 pad 32: (no net) -> /R2
- U3 pad 33: (no net) -> /R3
- U3 pad 34: (no net) -> /R4
- U3 pad 35: (no net) -> /R5
- U3 pad 36: (no net) -> /R6
- U3 pad 37: (no net) -> /R7
- U3 pad 38: (no net) -> Net-(U3-DVDD)
- U3 pad 39: (no net) -> /GND
- U3 pad 4: (no net) -> +3.3V
- U3 pad 40: (no net) -> unconnected-(U3-CTL1-Pad40)
- U3 pad 41: (no net) -> unconnected-(U3-CTL2-Pad41)
- U3 pad 42: (no net) -> unconnected-(U3-CTL3-Pad42)
- U3 pad 43: (no net) -> Net-(U3-OVDD)
- U3 pad 44: (no net) -> /PIXCLK
- U3 pad 45: (no net) -> /GND
- U3 pad 46: (no net) -> /DISPEN
- U3 pad 47: (no net) -> /VSYNC
- U3 pad 48: (no net) -> /HSYNC
- U3 pad 49: (no net) -> unconnected-(U3-QO0-Pad49)
- U3 pad 5: (no net) -> /GND
- U3 pad 50: (no net) -> unconnected-(U3-QO1-Pad50)
- U3 pad 51: (no net) -> unconnected-(U3-QO2-Pad51)
- U3 pad 52: (no net) -> unconnected-(U3-QO3-Pad52)
- U3 pad 53: (no net) -> unconnected-(U3-QO4-Pad53)
- U3 pad 54: (no net) -> unconnected-(U3-QO5-Pad54)
- U3 pad 55: (no net) -> unconnected-(U3-QO6-Pad55)
- U3 pad 56: (no net) -> unconnected-(U3-QO7-Pad56)
- U3 pad 57: (no net) -> Net-(U3-OVDD)
- U3 pad 58: (no net) -> /GND
- U3 pad 59: (no net) -> unconnected-(U3-QO8-Pad59)
- U3 pad 6: (no net) -> Net-(U3-DVDD)
- U3 pad 60: (no net) -> unconnected-(U3-QO9-Pad60)
- U3 pad 61: (no net) -> unconnected-(U3-QO10-Pad61)
- U3 pad 62: (no net) -> unconnected-(U3-QO11-Pad62)
- U3 pad 63: (no net) -> unconnected-(U3-QO12-Pad63)
- U3 pad 64: (no net) -> unconnected-(U3-QO13-Pad64)
- U3 pad 65: (no net) -> unconnected-(U3-QO14-Pad65)
- U3 pad 66: (no net) -> unconnected-(U3-QO15-Pad66)
- U3 pad 67: (no net) -> Net-(U3-DVDD)
- U3 pad 68: (no net) -> /GND
- U3 pad 69: (no net) -> unconnected-(U3-QO16-Pad69)
- U3 pad 7: (no net) -> +3.3V
- U3 pad 70: (no net) -> unconnected-(U3-QO17-Pad70)
- U3 pad 71: (no net) -> unconnected-(U3-QO18-Pad71)
- U3 pad 72: (no net) -> unconnected-(U3-QO19-Pad72)
- U3 pad 73: (no net) -> unconnected-(U3-QO20-Pad73)
- U3 pad 74: (no net) -> unconnected-(U3-QO21-Pad74)
- U3 pad 75: (no net) -> unconnected-(U3-QO22-Pad75)
- U3 pad 76: (no net) -> /GND
- U3 pad 77: (no net) -> unconnected-(U3-QO23-Pad77)
- U3 pad 78: (no net) -> Net-(U3-OVDD)
- U3 pad 79: (no net) -> /GND
- U3 pad 8: (no net) -> /ACTIVE
- U3 pad 80: (no net) -> Net-(U3-RX2+)
- U3 pad 81: (no net) -> Net-(U3-RX2-)
- U3 pad 82: (no net) -> Net-(U3-AVDD)
- U3 pad 83: (no net) -> /GND
- U3 pad 84: (no net) -> Net-(U3-AVDD)
- U3 pad 85: (no net) -> Net-(U3-RX1+)
- U3 pad 86: (no net) -> Net-(U3-RX1-)
- U3 pad 87: (no net) -> /GND
- U3 pad 88: (no net) -> Net-(U3-AVDD)
- U3 pad 89: (no net) -> /GND
- U3 pad 9: (no net) -> /PWRON_D
- U3 pad 90: (no net) -> Net-(U3-RX0+)
- U3 pad 91: (no net) -> Net-(U3-RX0-)
- U3 pad 92: (no net) -> /GND
- U3 pad 93: (no net) -> Net-(U3-RXC+)
- U3 pad 94: (no net) -> Net-(U3-RXC-)
- U3 pad 95: (no net) -> Net-(U3-AVDD)
- U3 pad 96: (no net) -> unconnected-(U3-EXT_RES-Pad96)
- U3 pad 97: (no net) -> Net-(U3-PVDD)
- U3 pad 98: (no net) -> /GND
- U3 pad 99: (no net) -> Net-(U3-DVDD)
- U5 pad 1: (no net) -> /GND
- U5 pad 2: (no net) -> Net-(U5-SW)
- U5 pad 3: (no net) -> 7V
- U5 pad 4: (no net) -> Net-(U5-VFB)
- U5 pad 5: (no net) -> 7V
- U5 pad 6: (no net) -> Net-(U5-VBST)
- U6 pad 1: (no net) -> 12V
- U6 pad 2: (no net) -> /PWM
- U6 pad 3: (no net) -> Net-(D1-ANODE)
- U6 pad 4: (no net) -> /GND
- U6 pad 5: (no net) -> Net-(U6-COMP)
- U6 pad 6: (no net) -> /LEDK
- U7 pad 1: (no net) -> /GND
- U7 pad 2: (no net) -> Net-(U7-SW)
- U7 pad 3: (no net) -> 7V
- U7 pad 4: (no net) -> Net-(U7-VFB)
- U7 pad 5: (no net) -> 7V
- U7 pad 6: (no net) -> Net-(U7-VBST)
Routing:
- net (no net): track 2667.7 -> 0.00 mm, vias 495 -> 0
- net +3.3V: track 0.00 -> 242.0 mm, vias 0 -> 12
- net /PWRON: track 0.00 -> 101.7 mm, vias 0 -> 2
- net +5V: track 0.00 -> 89.1 mm, vias 0 -> 5
- net /Rasberry PI (SPI clock input): track 0.00 -> 74.2 mm, vias 0 -> 2
- net /PWRON_D: track 0.00 -> 74.1 mm, vias 0 -> 2
- net Net-(U3-OVDD): track 0.00 -> 70.9 mm, vias 0 -> 4
- net /Rasberry PI (SPI output): track 0.00 -> 66.9 mm, vias 0 -> 2
- net /Rasberry PI (chip select): track 0.00 -> 63.8 mm, vias 0 -> 2
- net /Rasberry PI (SPI input): track 0.00 -> 59.2 mm, vias 0 -> 2
- net 7V: track 0.00 -> 58.7 mm, vias 0 -> 3
- net /Rasberry PI (TX interupt active low): track 0.00 -> 47.3 mm, vias 0 -> 2
- net Net-(U3-DVDD): track 0.00 -> 47.0 mm, vias 0 -> 3
- net /Rasberry PI (RX interupt active low): track 0.00 -> 43.5 mm, vias 0 -> 2
- net Net-(J3-Pad5): track 0.00 -> 43.3 mm, vias 0 -> 1
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- added copper zone on B.Cu, net /GND
- added copper zone on F.Cu, net /GND
- added copper zone on B.Cu, net DGND
- added copper zone on F.Cu, net DGND
- removed copper zone on B.Cu, net (none)
- removed copper zone on F.Cu, net (none)
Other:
- board size 170.6 x 99.2 mm -> 149.1 x 102.3 mm
